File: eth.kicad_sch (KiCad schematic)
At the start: 66 parts, among them U23 KSZ9131RNXC, U24 74AUP2G132, U25 TXU0304BQAR, Y5 Resonator_25MHz_ECX-1247Q

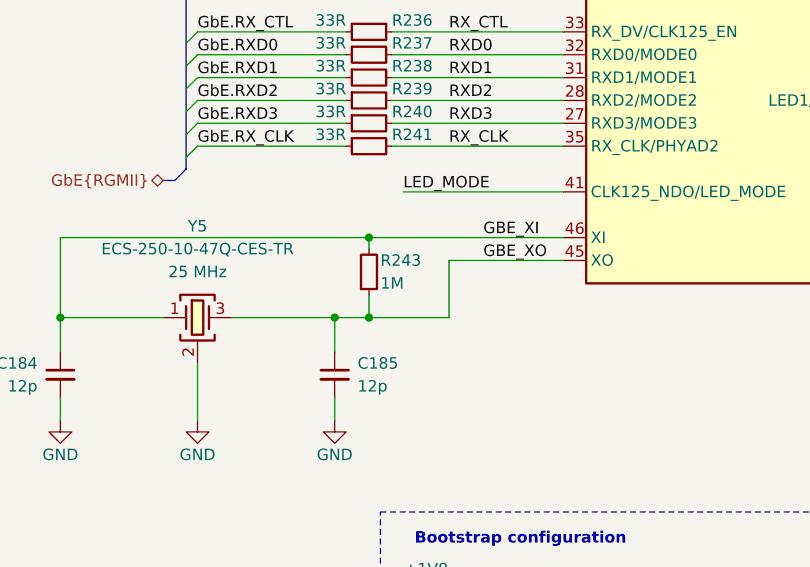
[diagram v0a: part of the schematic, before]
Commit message: [#101340] Reduce number of unique R MPNs
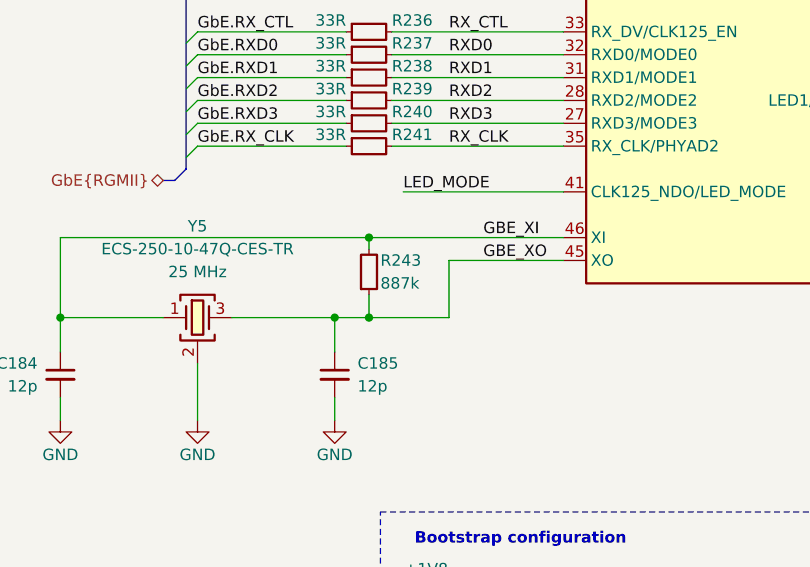
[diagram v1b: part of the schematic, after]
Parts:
- R243: value R_1M_0402 -> R_887k_0402; symbol antmicroResistors0402:R_1M_0402 -> antmicroResistors0402:R_887k_0402; MPN CR0402-FX-1004GLF -> ERJ-2RKF8873X; Manufacturer Bourns -> Panasonic; Val 1M -> 887k
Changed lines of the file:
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@@
 	)
 	(symbol
-		(lib_id "antmicroResistors0402:R_1M_0402")
+		(lib_id "antmicroResistors0402:R_887k_0402")
 		(at 166.37 179.07 90)
 		(unit 1)
@@
 			)
 		)
-		(property "Value" "R_1M_0402"
+		(property "Value" "R_887k_0402"
 			(at 179.07 158.75 0)
 			(hide yes)
@@
 			)
 		)
-		(property "Datasheet" "https://www.bourns.com/docs/product-datasheets/cr.pdf"
+		(property "Datasheet" "https://eu.mouser.com/datasheet/2/315/AOA0000C304-1149620.pdf"
 			(at 184.15 158.75 0)
 			(hide yes)
@@
 			)
 		)
-		(property "Description" "SMD Chip Resistor, 1 Mohm, ± 1%, 62.5 mW, 0402 [1005 Metric], Thick Film, General Purpose"
+		(property "Description" "SMD Chip Resistor"
 			(at 166.37 179.07 0)
 			(hide yes)
@@
 			)
 		)
-		(property "Manufacturer" "Bourns"
+		(property "Manufacturer" "Panasonic"
 			(at 189.23 158.75 0)
 			(hide yes)
@@
 			)
 		)
-		(property "MPN" "CR0402-FX-1004GLF"
+		(property "MPN" "ERJ-2RKF8873X"
 			(at 186.69 158.75 0)
 			(hide yes)
@@
 			)
 		)
-		(property "Val" "1M"
+		(property "Val" "887k"
 			(at 167.64 177.8001 90)
 			(show_name no)

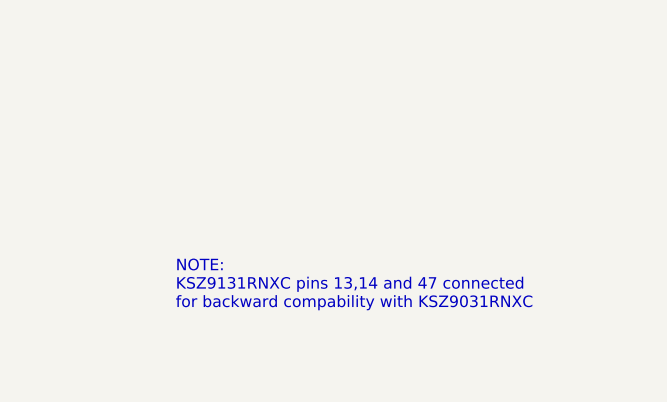
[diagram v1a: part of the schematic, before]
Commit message: [#101340] Update date on SCH and PCB
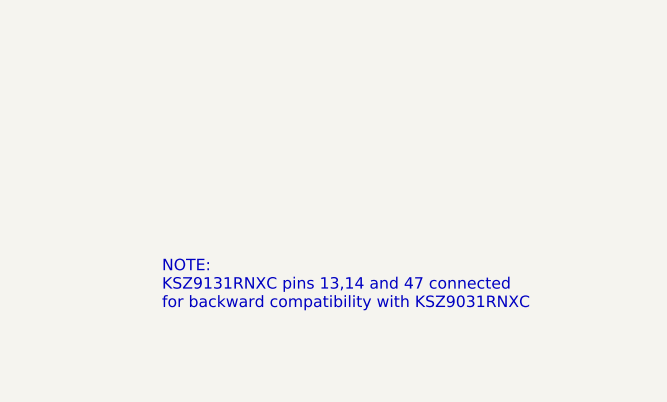
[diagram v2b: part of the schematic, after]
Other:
- note added: "NOTE: KSZ9131RNXC pins 13,14 and 47 connected for backward compatibility with KSZ9031RNXC"
- note removed: "NOTE: KSZ9131RNXC pins 13,14 and 47 connected for backward compability with KSZ9031RNXC"
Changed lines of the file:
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@@
 	(title_block
 		(title "altera-modular-agilex-5-dc-scm")
-		(date "2026-07-13")
+		(date "2026-07-24")
 		(rev "1.0.0")
 		(company "Altera")
@@
 		)
 	)
-	(text "NOTE:\nKSZ9131RNXC pins 13,14 and 47 connected \nfor backward compability with KSZ9031RNXC"
+	(text "NOTE:\nKSZ9131RNXC pins 13,14 and 47 connected \nfor backward compatibility with KSZ9031RNXC"
 		(exclude_from_sim no)
-		(at 362.458 250.952 0)
+		(at 360.934 250.952 0)
 		(effects
 			(font
